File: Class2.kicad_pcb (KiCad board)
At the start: 2 copper layers, 110 x 110 mm, 36 parts, among them J1 USB_C_Receptacle, J2 Conn_01x02_Pin, J3 Conn_ARM_JTAG_SWD_10, U1 STM32G030F6P6, U2 LR4054, U3 TPS613222ADBZ, U4 AMS1117-3.3, U5 MCP601R, U6 MCP4017-xxxxLT

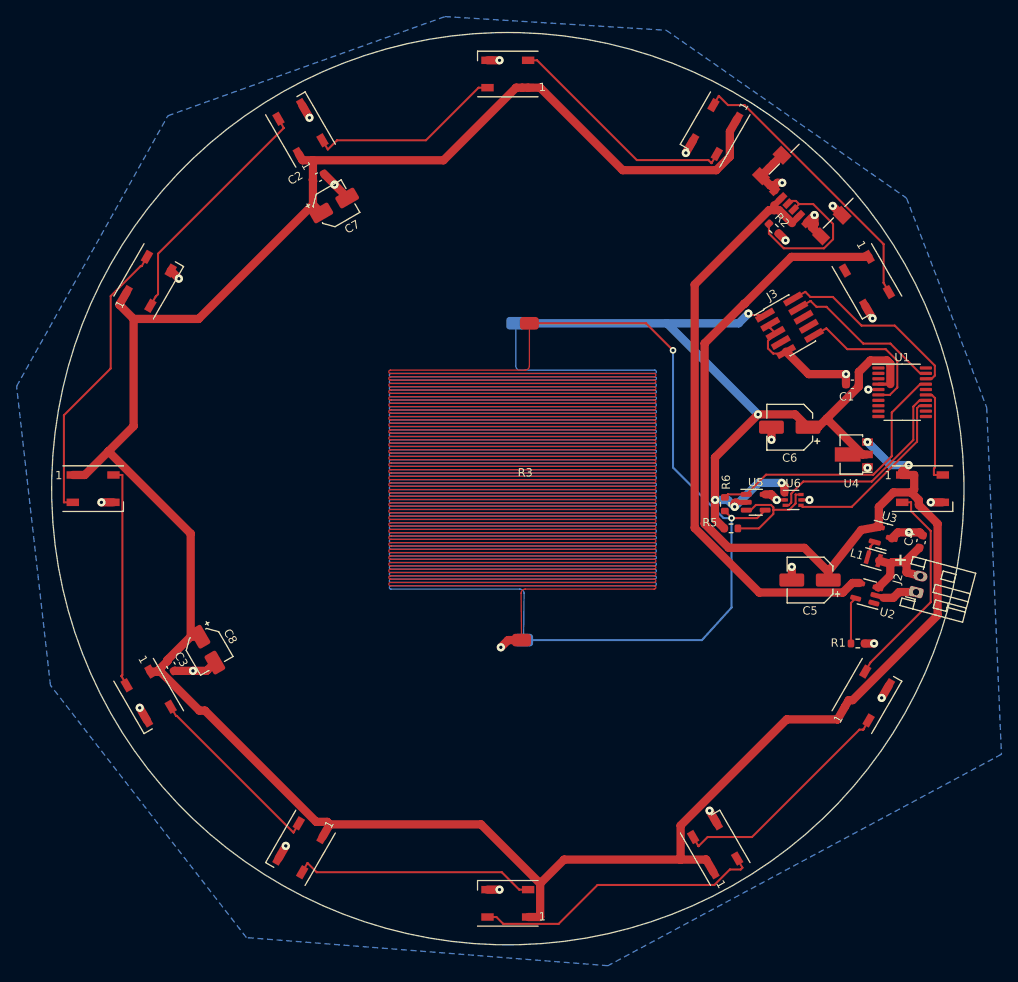
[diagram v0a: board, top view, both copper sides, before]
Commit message: add power switch, cleanups
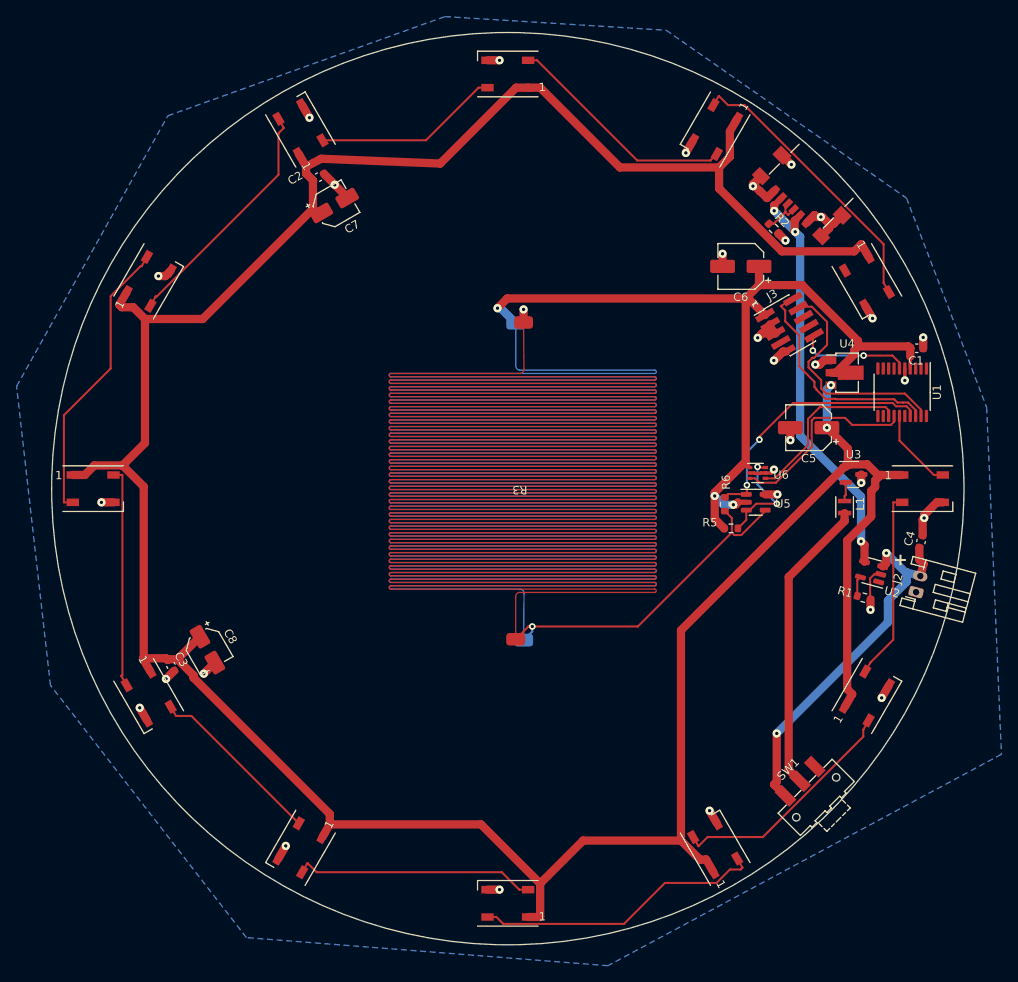
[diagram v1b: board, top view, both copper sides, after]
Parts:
- added SW1: SW_SPST, Button_Switch_SMD:SW_SPDT_CK-JS102011SAQN, F.Cu at (137.2, 137.2)
- R5: value 20k -> 9k1
- moved C6 20.3 mm to (128.1, 73.2)
- moved C5 18.4 mm to (136.3, 92.7)
- moved U4 9.87 mm to (140.9, 86.0), turned to 0 degrees
- moved C1 8.90 mm to (149.3, 83.1), turned to 0 degrees
- moved U3 8.34 mm to (141.7, 98.3), turned to 0 degrees
- moved L1 7.16 mm to (140.6, 102.2), turned to 90 degrees
- moved R1 5.57 mm to (142.9, 113.1), turned to -15 degrees
- moved U6 5.38 mm to (130.1, 98.1)
- moved U2 2.62 mm to (143.9, 110.0)
- moved R3 1.28 mm to (101.5, 99.7), turned to 180 degrees
- turned U1 to -90 degrees
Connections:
- L1 pad 1: /VBat -> /VBat_switched
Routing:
- net Net-(U5--): track 85.6 -> 41.9 mm, vias 2 -> 1
- net /VBat_switched: track 0.00 -> 35.7 mm
- net /VBat: track 12.3 -> 44.7 mm, vias 0 -> 2
- net +5V: track 401.0 -> 378.2 mm
- net /VUSB: track 72.2 -> 51.1 mm, vias 0 -> 3
- net Net-(J1-CC1): track 19.6 -> 5.15 mm
- net /SWCLK: track 19.2 -> 27.9 mm
- net GND: track 80.7 -> 72.6 mm, vias 28 -> 31
- net /~{RST}: track 17.8 -> 13.6 mm, vias 0 -> 2
- net /SWDIO: track 23.5 -> 27.3 mm
- net Net-(U2-PROG): track 5.70 -> 2.44 mm
- net Net-(D1-DOUT): track 25.6 -> 22.8 mm
- net +3V3: track 107.2 -> 105.0 mm, vias 5 -> 3
- net /LED_Data: track 11.7 -> 9.91 mm
- net /trans: track 33.0 -> 31.3 mm, vias 0 -> 2
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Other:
- board text added: "1"

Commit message: update board to use instrumentation amp
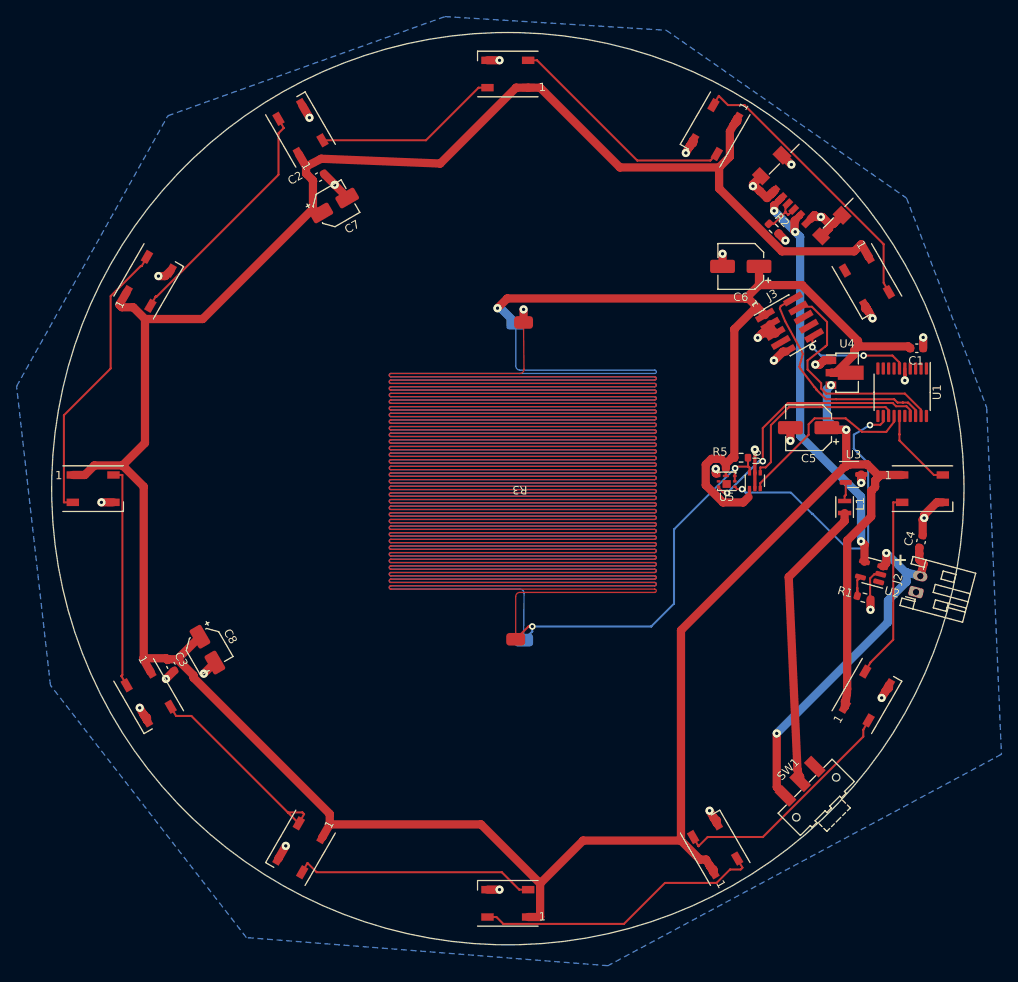
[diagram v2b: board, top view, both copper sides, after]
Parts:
- removed R6: 510k, Resistor_SMD:R_0603_1608Metric
- U5: value MCP601R -> INA350; footprint Package_TO_SOT_SMD:SOT-23-5 -> Package_SON:Texas_DQK
- moved R5 8.61 mm to (128.1, 96.3)
- moved U5 4.32 mm to (126.4, 99.1), turned to 180 degrees
- moved U6 0.98 mm to (129.8, 99.0), turned to 90 degrees
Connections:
- R3 pad 2: Net-(U5--) -> Net-(U5-+)
- R4 pad 1: Net-(U5--) -> Net-(U5-+)
- U1 pad 12: unconnected-(U1-PA5-Pad12) -> /Gain Select
- U5 pad 1: /trans -> /Gain Select
- U5 pad 2: +3V3 -> Net-(U5-+)
- U5 pad 4: Net-(U5--) -> GND
- U5 pad 5: GND -> unconnected-(U5-Ref-Pad5)
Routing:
- net Net-(U5--): track 41.9 -> 0.00 mm, vias 1 -> 0
- net /Gain Select: track 0.00 -> 38.4 mm, vias 0 -> 2
- net Net-(U5-+): track 13.0 -> 47.5 mm
- net GND: track 72.6 -> 80.0 mm
- net +5V: track 378.2 -> 383.9 mm
- net Net-(D4-DIN): track 21.4 -> 24.8 mm
- net +3V3: track 105.0 -> 102.5 mm, vias 3 -> 1
- net /sda: track 21.1 -> 22.8 mm
- net Net-(D2-DOUT): track 28.8 -> 30.4 mm
- net Net-(D10-DIN): track 34.5 -> 35.9 mm
- net /scl: track 23.9 -> 22.8 mm
- net Net-(D1-DOUT): track 22.8 -> 23.8 mm
- net /SWDIO: track 27.3 -> 28.2 mm
- net Net-(U2-PROG): track 2.44 -> 3.32 mm
- net Net-(D11-DIN): track 28.1 -> 28.9 mm
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
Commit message: production
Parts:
- removed R3, R4: ~, Sensor:strain_gauge
- removed R5: 9k1, Resistor_SMD:R_0603_1608Metric
- removed U5: INA350, Package_SON:Texas_DQK
- removed U6: MCP4017-xxxxLT, Package_TO_SOT_SMD:SOT-363_SC-70-6
- J1: footprint Connector_USB:USB_C_Receptacle_GCT_USB4135-GF-A_6P_TopMnt_Horizontal -> Connector_USB:USB_C_Receptacle_HRO_TYPE-C-31-M-12
- L1: footprint Inductor_SMD:L_Murata_DFE201610P -> Inductor_SMD:L_Vishay_IHLP-2020
- U3: value TPS613222ADBZ -> TPS613222ADBV; footprint Package_TO_SOT_SMD:SOT-23 -> Package_TO_SOT_SMD:SOT-23-5
- moved L1 4.21 mm to (137.3, 104.8)
- moved R2 3.59 mm to (128.7, 67.5), turned to 135 degrees
- moved J1 0.54 mm to (135.7, 63.9)
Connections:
- L1 pad 2: Net-(U3-SW) -> Net-(#FLG02-pwr)
- U3 pad 1: +5V -> Net-(#FLG02-pwr)
- U3 pad 2: Net-(U3-SW) -> GND
- U3 pad 3: GND -> unconnected-(U3-NC-Pad3)
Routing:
- net +3V3: track 102.5 -> 35.5 mm, vias 1 -> 0
- net Net-(U5-+): track 47.5 -> 0.00 mm, vias 2 -> 0
- net /Gain Select: track 38.4 -> 0.00 mm, vias 2 -> 0
- net +5V: track 383.9 -> 348.9 mm, vias 2 -> 6
- net /trans: track 31.6 -> 0.00 mm, vias 2 -> 0
- net /scl: track 22.8 -> 0.00 mm
- net /sda: track 22.8 -> 0.00 mm
- net GND: track 80.0 -> 63.4 mm, vias 31 -> 25
- net Net-(#FLG02-pwr): track 0.00 -> 8.29 mm
- net Net-(J1-CC1): track 5.15 -> 13.1 mm, vias 0 -> 2
- net /VBat_switched: track 35.9 -> 30.6 mm
- net Net-(U3-SW): track 2.30 -> 0.00 mm
- net /LED_Data: track 9.91 -> 11.4 mm
- net Net-(D10-DIN): track 35.9 -> 37.0 mm
- net /VBat: track 45.2 -> 44.4 mm
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
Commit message: fix drc and erc
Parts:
- added D13: SD103, Diode_SMD:D_SOD-323F, F.Cu at (142.7, 103.6)
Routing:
- net /VUSB: track 52.4 -> 56.6 mm
- net +5V: track 348.9 -> 352.2 mm

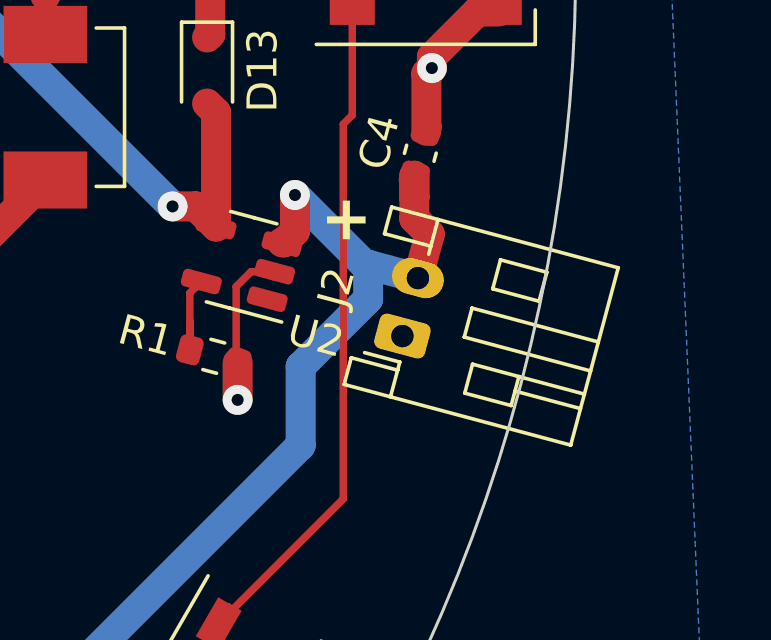
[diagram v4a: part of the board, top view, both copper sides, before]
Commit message: move battery connector to bottom
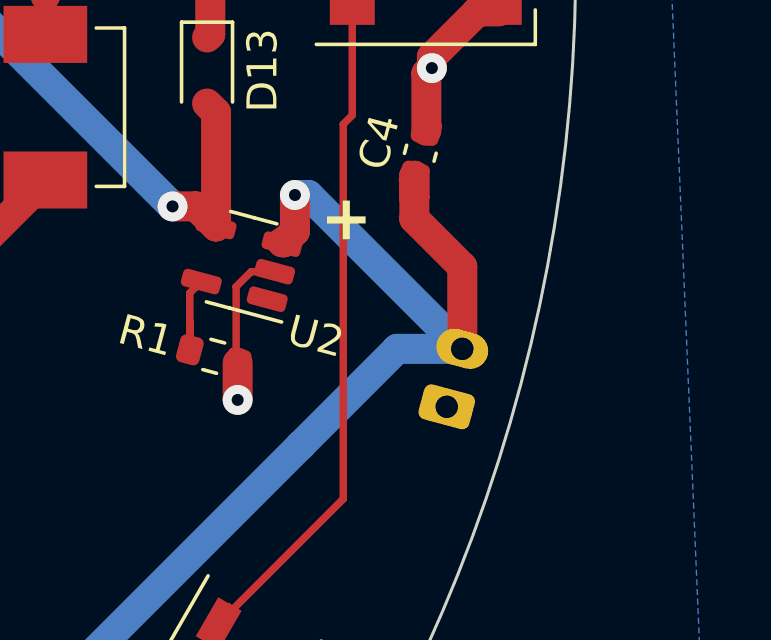
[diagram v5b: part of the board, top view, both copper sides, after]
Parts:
- J2: moved to B.Cu
- moved J2 2.78 mm to (150.7, 114.8)
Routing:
- net /VBat: track 44.4 -> 49.5 mm
